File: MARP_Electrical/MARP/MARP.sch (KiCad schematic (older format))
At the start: 26 parts, among them J1 CORTEX_DEBUGGER, P1 292304-1, U2 FT232RL, U3 ATSAMD21J18A-AU, U4 XBP9B-XCWT-002

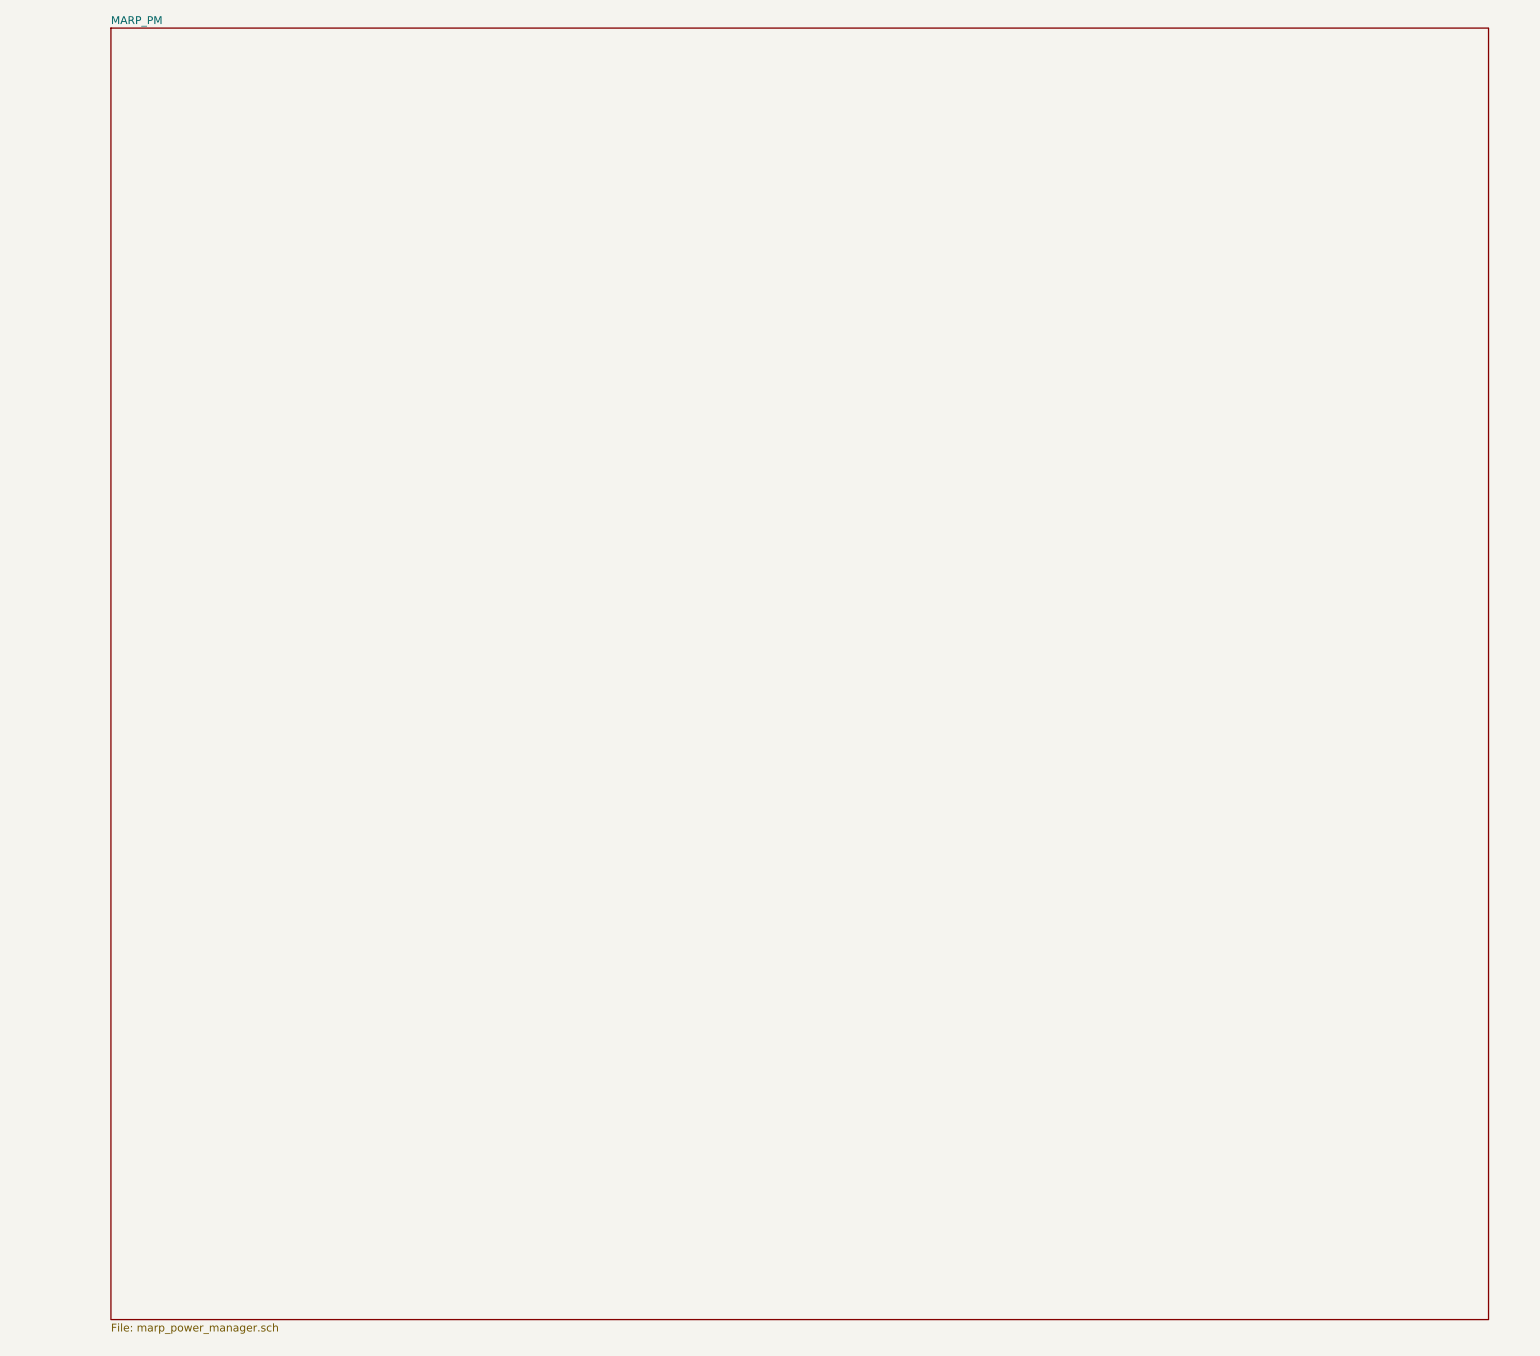
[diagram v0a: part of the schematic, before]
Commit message: decided on buck converter and thermocouple ic
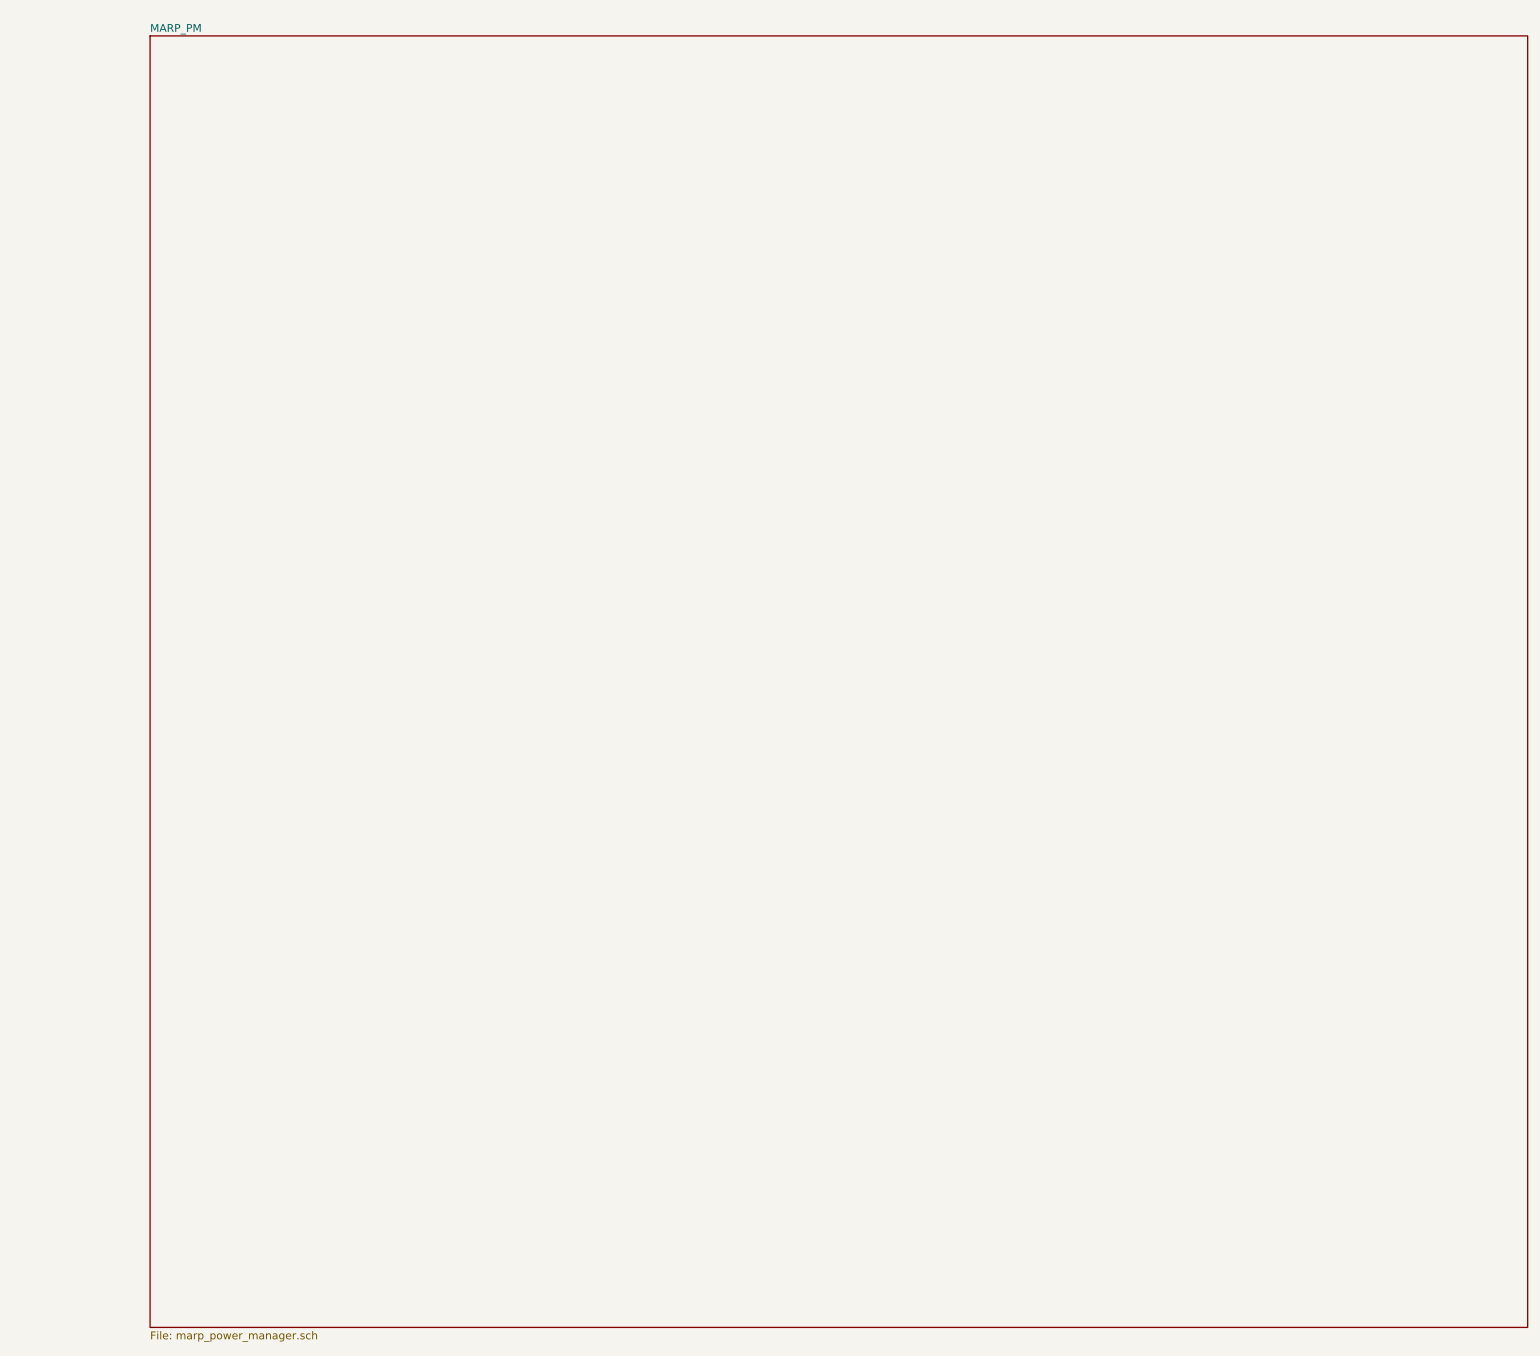
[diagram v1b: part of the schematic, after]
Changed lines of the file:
@@
 	1    0    0    -1
 $EndComp
-$Sheet
-S 11850 0    8800 8250
-U 5B7E0FCD
-F0 "MARP_PM" 50
-F1 "marp_power_manager.sch" 50
-$EndSheet
 $Comp
 L XBEE_900HP:XBP9B-XCWT-002 U4
@@
 	1    0    0    -1
 $EndComp
+$Sheet
+S 12100 50   8800 8250
+U 5B7E0FCD
+F0 "MARP_PM" 50
+F1 "marp_power_manager.sch" 50
+$EndSheet
 $EndSCHEMATC

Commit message: Added sd card holder, logic level shifter, fets for power source logic; removed old stuff
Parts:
- added D? (x2): LED, symbol Device:LED
- added Q? (x2): FQP27P06, digikey-footprints:TO-92-3, symbol dk_Transistors-FETs-MOSFETs-Single:FQP27P06
- added R?: 2200, symbol Device:R_Small
- added R?: 4700, symbol Device:R_Small
- added U?: CD74HC4050M, SOIC127P600X175-16N, symbol CD74HC4050M:CD74HC4050M
- P1: symbol Connector:292304-1 -> MARP-rescue:292304-1-Connector
- gave numbers to parts that had none: 12
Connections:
- net labels added: +3V3, +5V, -3V3
- wire segments 105 -> 131

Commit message: Started board layout; nearly finished with schematic
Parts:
- removed U?: CD74HC4050M, SOIC127P600X175-16N, symbol CD74HC4050M:CD74HC4050M
- added J?: MOLEX_47219-2001, MOLEX_47219-2001_0, symbol MOLEX_47219-2001:MOLEX_47219-2001
- added R? (x2): 10k, symbol Device:R_Small
- L2: value 10uF -> 220OHM
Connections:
- net labels added: I2C0_SCL, I2C0_SDA, SPI0_MISO, SPI0_MOSI, SPI0_SCK, ~SPI0_SDCARD_SS, ~SPI0_THERMO0_SS, ~SPI0_THERMO1_SS, ~SPI0_THERMO2_SS, ~SPI0_THERMO3_SS
- net labels removed: -3V3
- wire segments 131 -> 177
- no-connect marks 4 -> 6

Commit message: Added Thermocouple testing project
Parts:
- gave numbers to parts that had none: 9
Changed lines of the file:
@@
 $EndSheet
 $Comp
-L dk_Transistors-FETs-MOSFETs-Single:FQP27P06 Q?
+L dk_Transistors-FETs-MOSFETs-Single:FQP27P06 Q2
 U 1 1 5C1D1632
 P 3950 3500
-F 0 "Q?" H 4058 3553 60  0000 L CNN
+F 0 "Q2" H 4058 3553 60  0000 L CNN
 F 1 "FQP27P06" H 4058 3447 60  0000 L CNN
 F 2 "digikey-footprints:TO-92-3" H 4150 3700 60  0001 L CNN
@@
 $EndComp
 $Comp
-L dk_Transistors-FETs-MOSFETs-Single:FQP27P06 Q?
+L dk_Transistors-FETs-MOSFETs-Single:FQP27P06 Q1
 U 1 1 5C1D1E45
 P 1100 3650
-F 0 "Q?" H 1208 3703 60  0000 L CNN
+F 0 "Q1" H 1208 3703 60  0000 L CNN
 F 1 "FQP27P06" H 1208 3597 60  0000 L CNN
 F 2 "digikey-footprints:TO-92-3" H 1300 3850 60  0001 L CNN
@@
 $EndComp
 $Comp
-L Device:R_Small R?
+L Device:R_Small R8
 U 1 1 5C1D5CC0
 P 650 3150
-F 0 "R?" V 454 3150 50  0000 C CNN
+F 0 "R8" V 454 3150 50  0000 C CNN
 F 1 "2200" V 545 3150 50  0000 C CNN
 F 2 "" H 650 3150 50  0001 C CNN
@@
 $EndComp
 $Comp
-L Device:R_Small R?
+L Device:R_Small R7
 U 1 1 5C1DAC43
 P 550 3850
-F 0 "R?" H 609 3896 50  0000 L CNN
+F 0 "R7" H 609 3896 50  0000 L CNN
 F 1 "4700" H 609 3805 50  0000 L CNN
 F 2 "" H 550 3850 50  0001 C CNN
@@
 	550  3750 800  3750
 $Comp
-L power:GND #PWR?
+L power:GND #PWR01
 U 1 1 5C1E208D
 P 550 4000
-F 0 "#PWR?" H 550 3750 50  0001 C CNN
+F 0 "#PWR01" H 550 3750 50  0001 C CNN
 F 1 "GND" H 555 3827 50  0000 C CNN
 F 2 "" H 550 4000 50  0001 C CNN
@@
 	1100 3150 1400 3150
 $Comp
-L Device:LED D?
+L Device:LED D5
 U 1 1 5C215B6A
 P 1250 3300
-F 0 "D?" H 1242 3045 50  0000 C CNN
+F 0 "D5" H 1242 3045 50  0000 C CNN
 F 1 "LED" H 1242 3136 50  0000 C CNN
 F 2 "" H 1250 3300 50  0001 C CNN
@@
 Connection ~ 1500 3300
 $Comp
-L MAX31855:+5V #P+?
+L MAX31855:+5V #P+01
 U 1 1 5C231E45
 P 1800 3300
-F 0 "#P+?" H 1800 3300 50  0001 C CNN
+F 0 "#P+01" H 1800 3300 50  0001 C CNN
 F 1 "+5V" V 1800 3369 59  0000 L CNN
 F 2 "" H 1800 3300 50  0001 C CNN
@@
 $EndComp
 $Comp
-L power:+3V3 #PWR?
+L power:+3V3 #PWR03
 U 1 1 5C232AA5
 P 4150 3250
-F 0 "#PWR?" H 4150 3100 50  0001 C CNN
+F 0 "#PWR03" H 4150 3100 50  0001 C CNN
 F 1 "+3V3" V 4165 3378 50  0000 L CNN
 F 2 "" H 4150 3250 50  0001 C CNN
@@
 $EndComp
 $Comp
-L Device:LED D?
+L Device:LED D6
 U 1 1 5C232BB7
 P 4050 3050
-F 0 "D?" V 4088 2933 50  0000 R CNN
+F 0 "D6" V 4088 2933 50  0000 R CNN
 F 1 "LED" V 3997 2933 50  0000 R CNN
 F 2 "" H 4050 3050 50  0001 C CNN
@@
 	7250 1750 7950 1750
 $Comp
-L MOLEX_47219-2001:MOLEX_47219-2001 J?
+L MOLEX_47219-2001:MOLEX_47219-2001 J2
 U 1 1 5C1B24FE
 P 800 4600
-F 0 "J?" H 1288 4476 50  0000 C CNN
+F 0 "J2" H 1288 4476 50  0000 C CNN
 F 1 "MOLEX_47219-2001" H 800 4600 50  0001 L BNN
 F 2 "MOLEX_47219-2001_0" H 800 4600 50  0001 L BNN
@@
 	1600 6000 1750 6000
 $Comp
-L power:GND #PWR?
+L power:GND #PWR02
 U 1 1 5C1D3B3C
 P 1750 6000
-F 0 "#PWR?" H 1750 5750 50  0001 C CNN
+F 0 "#PWR02" H 1750 5750 50  0001 C CNN
 F 1 "GND" V 1755 5872 50  0000 R CNN
 F 2 "" H 1750 6000 50  0001 C CNN
@@
 	1750 6600 1750 6800
 $Comp
-L MAX31855:+3V3 #+3V3?
+L MAX31855:+3V3 #+3V0301
 U 1 1 5C19B06E
 P 1800 5600
-F 0 "#+3V3?" H 1800 5600 50  0001 C CNN
+F 0 "#+3V0301" H 1800 5600 50  0001 C CNN
 F 1 "+3V3" V 1800 5669 59  0000 L CNN
 F 2 "" H 1800 5600 50  0001 C CNN
@@
 $EndComp
 $Comp
-L MAX31855:+3V3 #+3V3?
+L MAX31855:+3V3 #+3V0305
 U 1 1 5C19BD33
 P 5150 2150
-F 0 "#+3V3?" H 5150 2150 50  0001 C CNN
+F 0 "#+3V0305" H 5150 2150 50  0001 C CNN
 F 1 "+3V3" H 5150 2271 59  0000 C CNN
 F 2 "" H 5150 2150 50  0001 C CNN
@@
 $EndComp
 $Comp
-L MAX31855:+3V3 #+3V3?
+L MAX31855:+3V3 #+3V0306
 U 1 1 5C19C2E1
 P 7700 1600
-F 0 "#+3V3?" H 7700 1600 50  0001 C CNN
+F 0 "#+3V0306" H 7700 1600 50  0001 C CNN
 F 1 "+3V3" V 7700 1669 59  0000 L CNN
 F 2 "" H 7700 1600 50  0001 C CNN
@@
 	2000 5200 1600 5200
 $Comp
-L MAX31855:+3V3 #+3V3?
+L MAX31855:+3V3 #+3V0307
 U 1 1 5C1E2997
 P 10900 1000
-F 0 "#+3V3?" H 10900 1000 50  0001 C CNN
+F 0 "#+3V0307" H 10900 1000 50  0001 C CNN
 F 1 "+3V3" H 10900 1121 59  0000 C CNN
 F 2 "" H 10900 1000 50  0001 C CNN
@@
 $EndComp
 $Comp
-L MAX31855:+3V3 #+3V3?
+L MAX31855:+3V3 #+3V0302
 U 1 1 5C1E3BA9
 P 3400 5500
-F 0 "#+3V3?" H 3400 5500 50  0001 C CNN
+F 0 "#+3V0302" H 3400 5500 50  0001 C CNN
 F 1 "+3V3" V 3400 5569 59  0000 L CNN
 F 2 "" H 3400 5500 50  0001 C CNN
@@
 	4200 4150 5350 4150
 $Comp
-L Device:R_Small R?
+L Device:R_Small R10
 U 1 1 5C236068
 P 5000 3650
-F 0 "R?" H 5059 3696 50  0000 L CNN
+F 0 "R10" H 5059 3696 50  0000 L CNN
 F 1 "10k" H 5059 3605 50  0000 L CNN
 F 2 "" H 5000 3650 50  0001 C CNN
@@
 $EndComp
 $Comp
-L MAX31855:+3V3 #+3V3?
+L MAX31855:+3V3 #+3V0304
 U 1 1 5C236184
 P 4850 3550
-F 0 "#+3V3?" H 4850 3550 50  0001 C CNN
+F 0 "#+3V0304" H 4850 3550 50  0001 C CNN
 F 1 "+3V3" V 4800 3500 59  0000 L CNN
 F 2 "" H 4850 3550 50  0001 C CNN
@@
 	5000 3550 4950 3550
 $Comp
-L Device:R_Small R?
+L Device:R_Small R9
 U 1 1 5C248C59
 P 4150 3750
-F 0 "R?" H 4209 3796 50  0000 L CNN
+F 0 "R9" H 4209 3796 50  0000 L CNN
 F 1 "10k" H 4209 3705 50  0000 L CNN
 F 2 "" H 4150 3750 50  0001 C CNN
@@
 	4150 3850 5350 3850
 $Comp
-L MAX31855:+3V3 #+3V3?
+L MAX31855:+3V3 #+3V0303
 U 1 1 5C2BB330
 P 4400 3650
-F 0 "#+3V3?" H 4400 3650 50  0001 C CNN
+F 0 "#+3V0303" H 4400 3650 50  0001 C CNN
 F 1 "+3V3" V 4400 3550 59  0000 L CNN
 F 2 "" H 4400 3650 50  0001 C CNN

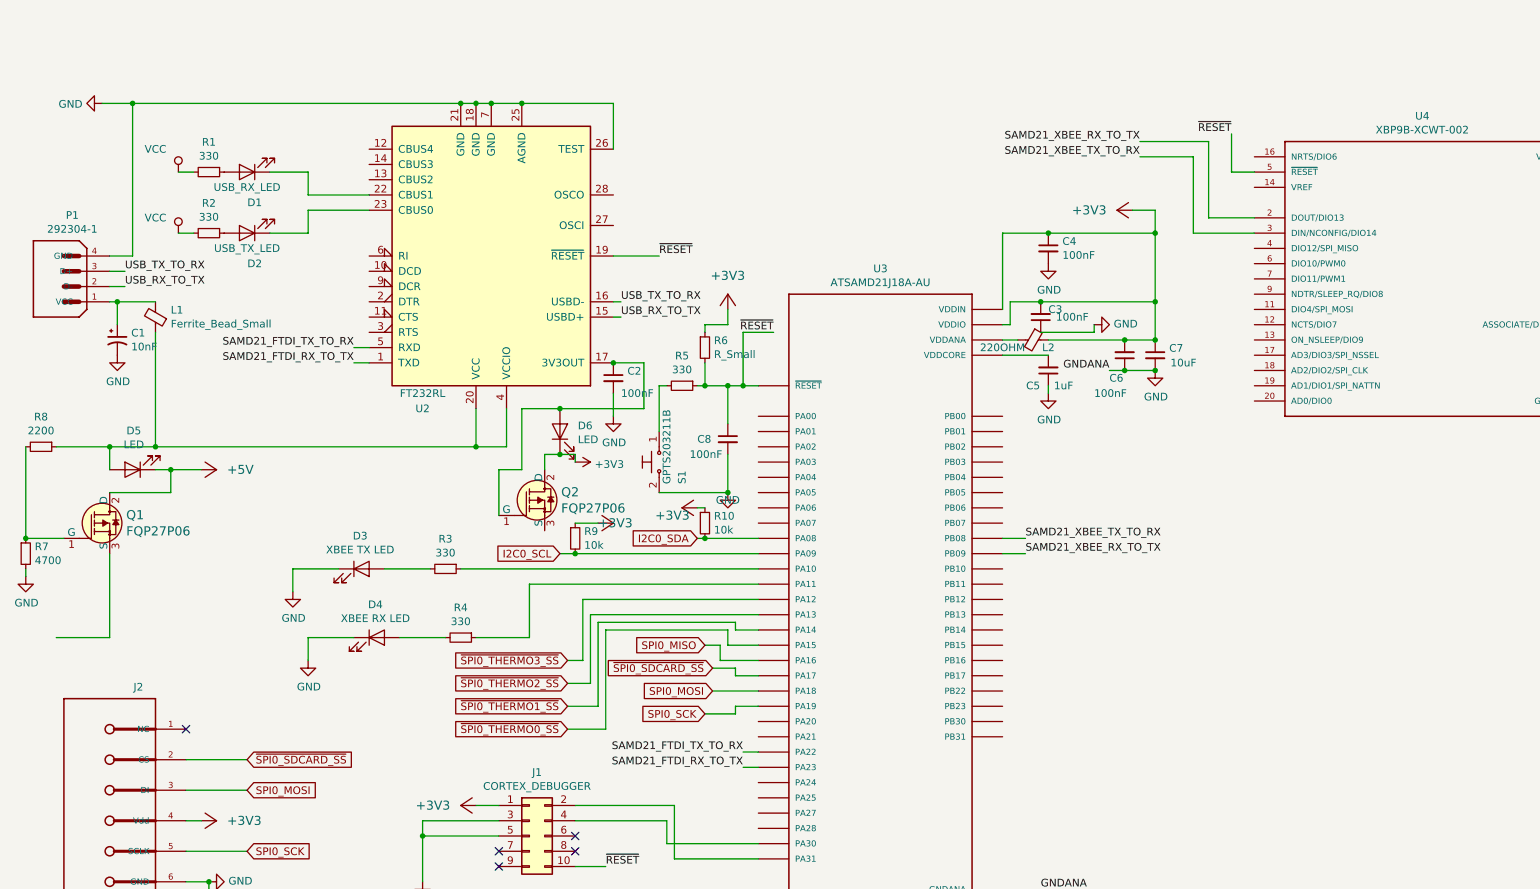
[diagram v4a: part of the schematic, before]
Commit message: added a python script for capacitor discharge analysis
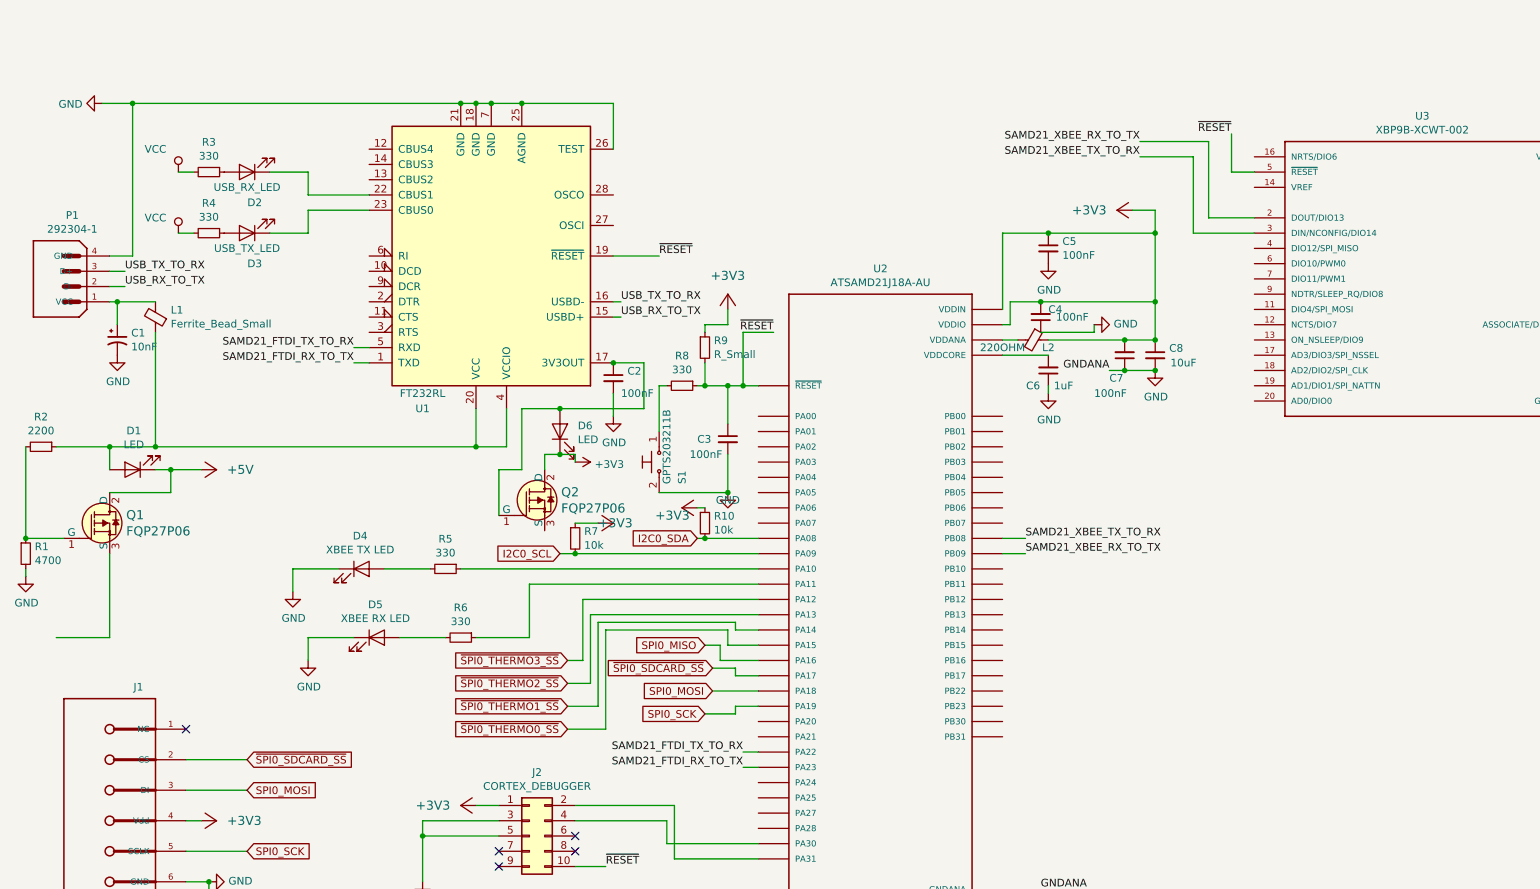
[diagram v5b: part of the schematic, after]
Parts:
- J1: renamed from J2; footprint MOLEX_47219-2001_0 -> (none)
- P1: footprint TE_292304-1 -> (none)
- U2: renamed from U3; footprint QFP50P1200X1200X120_64N -> (none)
- U3: renamed from U4; footprint DIP2200W51P200L3294H279Q20P -> (none)
- renumbered C8 to C3, C3 to C4, C4 to C5, C5 to C6, C6 to C7, C7 to C8, D5 to D1, D1 to D2, D2 to D3, D3 to D4, D4 to D5, J1 to J2, R7 to R1, R8 to R2, R1 to R3, R2 to R4, R3 to R5, R4 to R6, R9 to R7, R5 to R8, R6 to R9, U2 to U1
